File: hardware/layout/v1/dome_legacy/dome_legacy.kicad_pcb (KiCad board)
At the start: 4 copper layers, 13.6 x 13.6 mm, 7 parts, among them J1 CROWN_RISER, U1 LTR-390UV-01, U2 TSL25911FN, U3 GUVB-C31SM

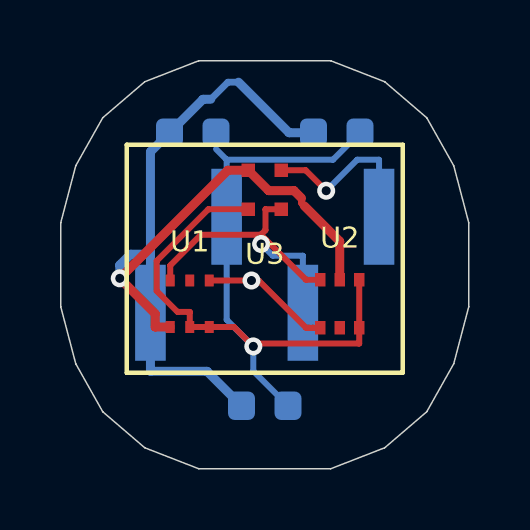
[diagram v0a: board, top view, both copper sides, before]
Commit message: Update dome PCB layout with manual reference and label placement, add Stock_Optional field for LTR-390UV-01 sensor to allow JLC assembly when in stock without failing release on shortage
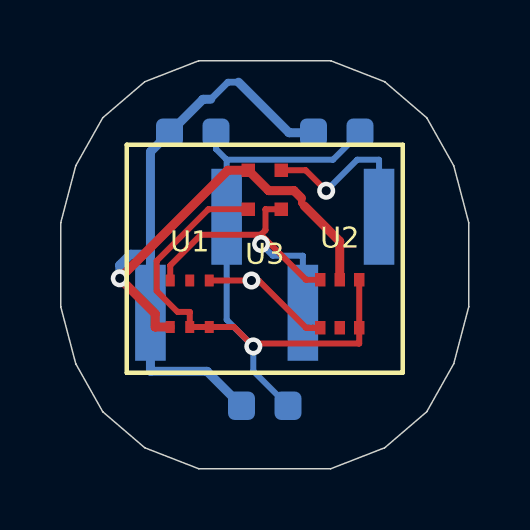
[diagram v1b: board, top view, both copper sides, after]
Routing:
- net GND: track 29.0 -> 29.5 mm
